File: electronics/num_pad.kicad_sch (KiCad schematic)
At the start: 37 parts, among them J10 Conn_01x05_Male, J9 Conn_01x05_Female, SW69 SW_SPST, SW70 SW_SPST, SW71 SW_SPST, SW72 SW_SPST, SW73 SW_SPST, SW74 SW_SPST, SW75 SW_SPST, SW76 SW_SPST, SW77 SW_SPST, SW78 SW_SPST, SW79 SW_SPST, SW80 SW_SPST, SW81 SW_SPST, SW82 SW_SPST, SW83 SW_SPST, SW84 SW_SPST, SW85 SW_SPST, U5 PCA9675PW

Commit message: finish matrix
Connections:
- net COL30: now also U5.16 (P13); no longer U5.13 (P10)
- net COL31: now also U5.15 (P12); no longer U5.14 (P11)
- net COL32: now also U5.14 (P11); no longer U5.15 (P12)
- net COL33: now also U5.13 (P10); no longer U5.16 (P13)
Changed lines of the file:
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@@
     (stroke (width 0) (type default) (color 0 0 0 0))
   )
+  (global_label "COL30" (shape input) (at 237.49 66.04 0) (fields_autoplaced)
+    (effects (font (size 1.27 1.27)) (justify left))
+    (property "Intersheet References" "${INTERSHEET_REFS}" (id 0) (at 245.9507 65.9606 0)
+      (effects (font (size 1.27 1.27)) (justify left) hide)
+    )
+  )
   (global_label "ROW30" (shape input) (at 55.88 101.6 180) (fields_autoplaced)
     (effects (font (size 1.27 1.27)) (justify right))
@@
     )
   )
-  (global_label "COL32" (shape input) (at 237.49 63.5 0) (fields_autoplaced)
-    (effects (font (size 1.27 1.27)) (justify left))
-    (property "Intersheet References" "${INTERSHEET_REFS}" (id 0) (at 245.9507 63.5794 0)
-      (effects (font (size 1.27 1.27)) (justify left) hide)
-    )
-  )
   (global_label "ROW34" (shape input) (at 96.52 165.1 180) (fields_autoplaced)
     (effects (font (size 1.27 1.27)) (justify right))
@@
     )
   )
+  (global_label "COL33" (shape input) (at 237.49 58.42 0) (fields_autoplaced)
+    (effects (font (size 1.27 1.27)) (justify left))
+    (property "Intersheet References" "${INTERSHEET_REFS}" (id 0) (at 245.9507 58.3406 0)
+      (effects (font (size 1.27 1.27)) (justify left) hide)
+    )
+  )
   (global_label "ROW30" (shape input) (at 96.52 101.6 180) (fields_autoplaced)
     (effects (font (size 1.27 1.27)) (justify right))
@@
     )
   )
-  (global_label "COL31" (shape input) (at 237.49 60.96 0) (fields_autoplaced)
-    (effects (font (size 1.27 1.27)) (justify left))
-    (property "Intersheet References" "${INTERSHEET_REFS}" (id 0) (at 245.9507 61.0394 0)
-      (effects (font (size 1.27 1.27)) (justify left) hide)
-    )
-  )
   (global_label "COL33" (shape input) (at 127 82.55 180) (fields_autoplaced)
     (effects (font (size 1.27 1.27)) (justify right))
@@
     )
   )
-  (global_label "COL30" (shape input) (at 237.49 58.42 0) (fields_autoplaced)
-    (effects (font (size 1.27 1.27)) (justify left))
-    (property "Intersheet References" "${INTERSHEET_REFS}" (id 0) (at 245.9507 58.4994 0)
-      (effects (font (size 1.27 1.27)) (justify left) hide)
-    )
-  )
   (global_label "~{INT}" (shape input) (at 237.49 45.72 0) (fields_autoplaced)
     (effects (font (size 1.27 1.27)) (justify left))
@@
     )
   )
-  (global_label "COL33" (shape input) (at 237.49 66.04 0) (fields_autoplaced)
-    (effects (font (size 1.27 1.27)) (justify left))
-    (property "Intersheet References" "${INTERSHEET_REFS}" (id 0) (at 245.9507 66.1194 0)
-      (effects (font (size 1.27 1.27)) (justify left) hide)
-    )
-  )
   (global_label "ROW33" (shape input) (at 76.2 149.86 180) (fields_autoplaced)
     (effects (font (size 1.27 1.27)) (justify right))
@@
     )
   )
+  (global_label "COL31" (shape input) (at 237.49 63.5 0) (fields_autoplaced)
+    (effects (font (size 1.27 1.27)) (justify left))
+    (property "Intersheet References" "${INTERSHEET_REFS}" (id 0) (at 245.9507 63.4206 0)
+      (effects (font (size 1.27 1.27)) (justify left) hide)
+    )
+  )
   (global_label "ROW33" (shape input) (at 201.93 66.04 180) (fields_autoplaced)
     (effects (font (size 1.27 1.27)) (justify right))
@@
       (effects (font (size 1.27 1.27)) (justify left) hide)
     )
+  )
+  (global_label "COL32" (shape input) (at 237.49 60.96 0) (fields_autoplaced)
+    (effects (font (size 1.27 1.27)) (justify left))
+    (property "Intersheet References" "${INTERSHEET_REFS}" (id 0) (at 245.9507 60.8806 0)
+      (effects (font (size 1.27 1.27)) (justify left) hide)
+    )

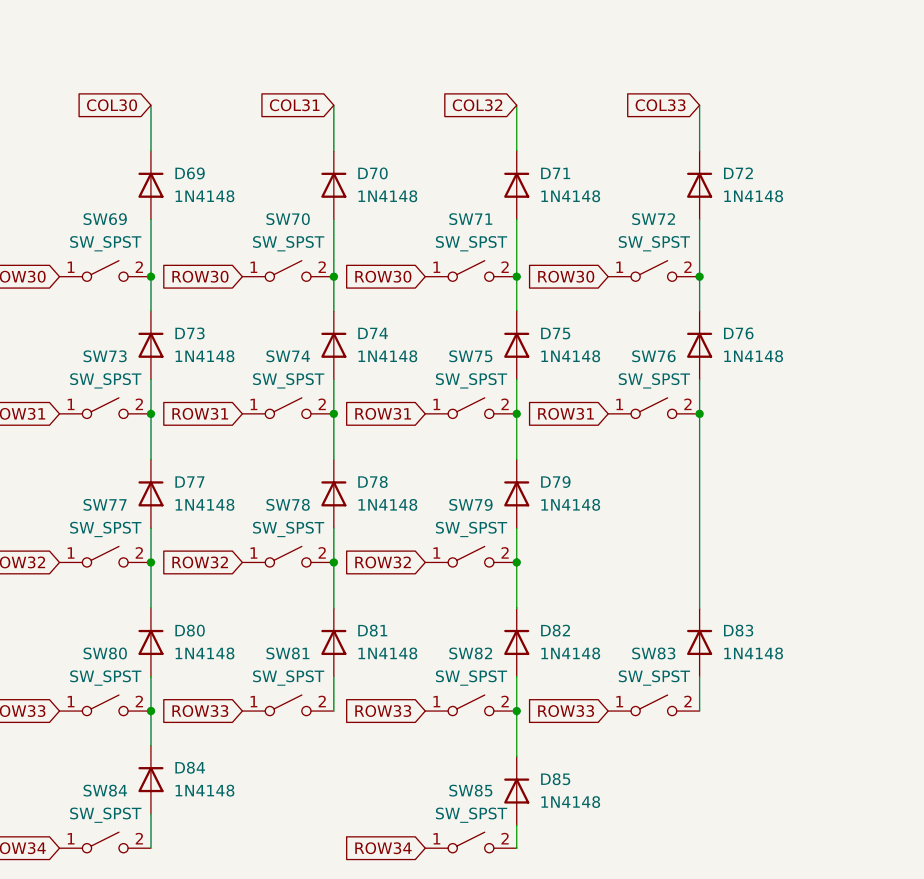
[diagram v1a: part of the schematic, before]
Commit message: update diode libraries
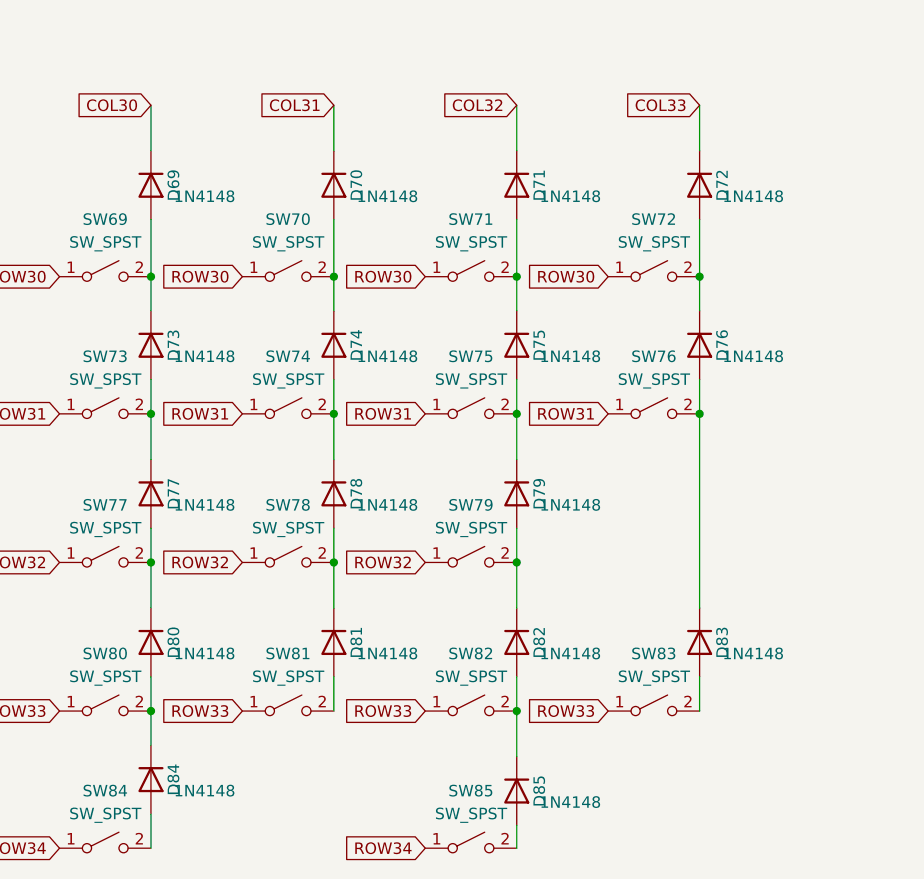
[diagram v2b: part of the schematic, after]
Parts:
- D69, D70, D71, D72, D73, D74, D75, D76, D77, D78, D79, D80, D81, D82, D83, D84, D85: symbol Diode:1N4148W -> 1N4148:1N4148

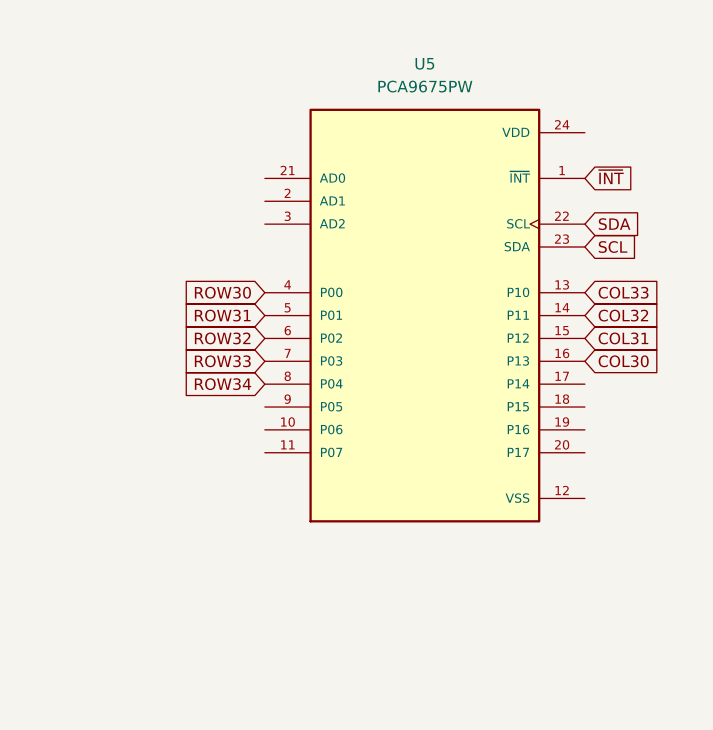
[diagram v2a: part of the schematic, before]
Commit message: add power and i2c addressing
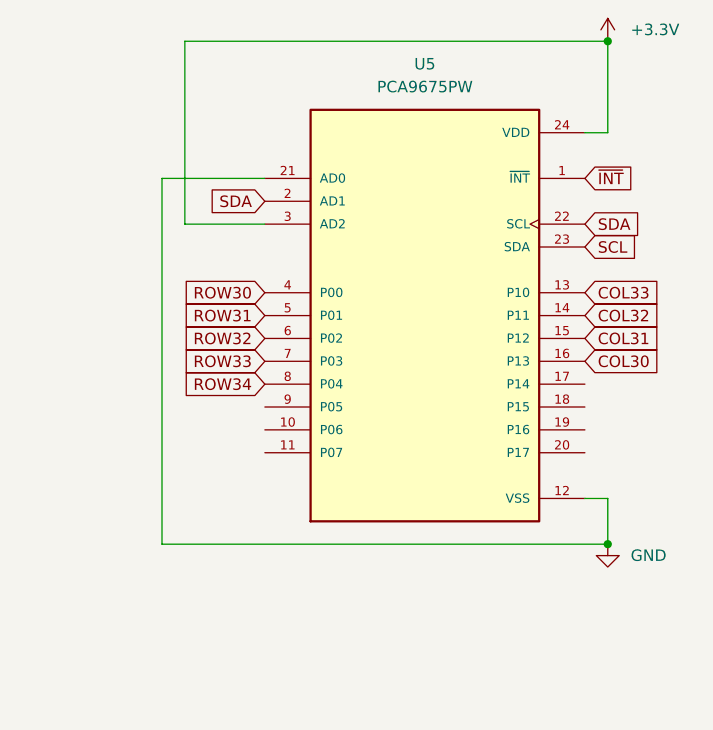
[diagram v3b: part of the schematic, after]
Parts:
- D69, D70, D71, D72, D73, D74, D75, D76, D77, D78, D79, D80, D81, D82, D83, D84, D85: footprint Diode_SMD:D_SOD-123 -> 1N4148:1N4148
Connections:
- net +3V3: now also U5.24 (VDD), U5.3 (AD2)
- net GND: now also U5.12 (VSS), U5.21 (AD0)
- net SDA: now also U5.2 (AD1)
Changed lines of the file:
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@@
   (junction (at 86.36 116.84) (diameter 0) (color 0 0 0 0)
   )
+  (junction (at 240.03 86.36) (diameter 0) (color 0 0 0 0)
+  )
   (junction (at 86.36 101.6) (diameter 0) (color 0 0 0 0)
   )
@@
   (junction (at 66.04 116.84) (diameter 0) (color 0 0 0 0)
   )
+  (junction (at 240.03 30.48) (diameter 0) (color 0 0 0 0)
+  )
   (wire (pts (xy 66.04 129.54) (xy 66.04 133.35))
     (stroke (width 0) (type default) (color 0 0 0 0))
   )
+  (wire (pts (xy 237.49 40.64) (xy 240.03 40.64))
+    (stroke (width 0) (type default) (color 0 0 0 0))
+  )
   (wire (pts (xy 106.68 129.54) (xy 106.68 133.35))
     (stroke (width 0) (type default) (color 0 0 0 0))
@@
     (stroke (width 0) (type default) (color 0 0 0 0))
   )
+  (wire (pts (xy 240.03 81.28) (xy 237.49 81.28))
+    (stroke (width 0) (type default) (color 0 0 0 0))
+  )
   (wire (pts (xy 106.68 82.55) (xy 106.68 87.63))
     (stroke (width 0) (type default) (color 0 0 0 0))
@@
     (stroke (width 0) (type default) (color 0 0 0 0))
   )
+  (wire (pts (xy 201.93 45.72) (xy 190.5 45.72))
+    (stroke (width 0) (type default) (color 0 0 0 0))
+  )
   (wire (pts (xy 106.68 101.6) (xy 106.68 105.41))
     (stroke (width 0) (type default) (color 0 0 0 0))
@@
     (stroke (width 0) (type default) (color 0 0 0 0))
   )
+  (wire (pts (xy 190.5 86.36) (xy 240.03 86.36))
+    (stroke (width 0) (type default) (color 0 0 0 0))
+  )
   (wire (pts (xy 127 82.55) (xy 127 87.63))
     (stroke (width 0) (type default) (color 0 0 0 0))
@@
     (stroke (width 0) (type default) (color 0 0 0 0))
   )
+  (wire (pts (xy 193.04 30.48) (xy 193.04 50.8))
+    (stroke (width 0) (type default) (color 0 0 0 0))
+  )
+  (wire (pts (xy 240.03 30.48) (xy 193.04 30.48))
+    (stroke (width 0) (type default) (color 0 0 0 0))
+  )
   (wire (pts (xy 66.04 146.05) (xy 66.04 149.86))
     (stroke (width 0) (type default) (color 0 0 0 0))
@@
   )
   (wire (pts (xy 86.36 95.25) (xy 86.36 101.6))
+    (stroke (width 0) (type default) (color 0 0 0 0))
+  )
+  (wire (pts (xy 240.03 86.36) (xy 240.03 81.28))
+    (stroke (width 0) (type default) (color 0 0 0 0))
+  )
+  (wire (pts (xy 190.5 45.72) (xy 190.5 86.36))
+    (stroke (width 0) (type default) (color 0 0 0 0))
+  )
+  (wire (pts (xy 193.04 50.8) (xy 201.93 50.8))
+    (stroke (width 0) (type default) (color 0 0 0 0))
+  )
+  (wire (pts (xy 240.03 40.64) (xy 240.03 30.48))
     (stroke (width 0) (type default) (color 0 0 0 0))
   )
@@
     )
   )
+  (global_label "SDA" (shape input) (at 201.93 48.26 180) (fields_autoplaced)
+    (effects (font (size 1.27 1.27)) (justify right))
+    (property "Intersheet References" "${INTERSHEET_REFS}" (id 0) (at 195.9488 48.1806 0)
+      (effects (font (size 1.27 1.27)) (justify right) hide)
+    )
+  )
   (global_label "~{INT}" (shape input) (at 237.49 45.72 0) (fields_autoplaced)
     (effects (font (size 1.27 1.27)) (justify left))
@@
       (effects (font (size 1.27 1.27)) (justify left))
     )
-    (property "Footprint" "Diode_SMD:D_SOD-123" (id 2) (at 81.915 91.44 0)
+    (property "Footprint" "1N4148:1N4148" (id 2) (at 81.915 91.44 0)
       (effects (font (size 1.27 1.27)) hide)
     )
@@
       (effects (font (size 1.27 1.27)) (justify left))
     )
-    (property "Footprint" "Diode_SMD:D_SOD-123" (id 2) (at 61.595 142.24 0)
+    (property "Footprint" "1N4148:1N4148" (id 2) (at 61.595 142.24 0)
       (effects (font (size 1.27 1.27)) hide)
     )
@@
       (effects (font (size 1.27 1.27)) (justify left))
     )
-    (property "Footprint" "Diode_SMD:D_SOD-123" (id 2) (at 81.915 125.73 0)
+    (property "Footprint" "1N4148:1N4148" (id 2) (at 81.915 125.73 0)
       (effects (font (size 1.27 1.27)) hide)
     )
@@
     (pin "2")
   )
+  (symbol (lib_id "power:GND") (at 240.03 86.36 0) (unit 1)
+    (in_bom yes) (on_board yes) (fields_autoplaced)
+    (property "Reference" "#PWR?" (id 0) (at 240.03 92.71 0)
+      (effects (font (size 1.27 1.27)) hide)
+    )
+    (property "Value" "GND" (id 1) (at 242.57 87.6299 0)
+      (effects (font (size 1.27 1.27)) (justify left))
+    )
+    (property "Footprint" "" (id 2) (at 240.03 86.36 0)
+      (effects (font (size 1.27 1.27)) hide)
+    )
+    (property "Datasheet" "" (id 3) (at 240.03 86.36 0)
+      (effects (font (size 1.27 1.27)) hide)
+    )
+    (pin "1")
+  )
   (symbol (lib_name "1N4148_11") (lib_id "1N4148:1N4148") (at 127 91.44 270) (unit 1)
     (in_bom yes) (on_board yes) (fields_autoplaced)
@@
       (effects (font (size 1.27 1.27)) (justify left))
     )
-    (property "Footprint" "Diode_SMD:D_SOD-123" (id 2) (at 122.555 91.44 0)
+    (property "Footprint" "1N4148:1N4148" (id 2) (at 122.555 91.44 0)
       (effects (font (size 1.27 1.27)) hide)
     )
@@
       (effects (font (size 1.27 1.27)) (justify left))
     )
-    (property "Footprint" "Diode_SMD:D_SOD-123" (id 2) (at 102.235 158.75 0)
+    (property "Footprint" "1N4148:1N4148" (id 2) (at 102.235 158.75 0)
       (effects (font (size 1.27 1.27)) hide)
     )
@@
       (effects (font (size 1.27 1.27)) (justify left))
     )
-    (property "Footprint" "Diode_SMD:D_SOD-123" (id 2) (at 61.595 157.48 0)
+    (property "Footprint" "1N4148:1N4148" (id 2) (at 61.595 157.48 0)
       (effects (font (size 1.27 1.27)) hide)
     )
@@
       (effects (font (size 1.27 1.27)) (justify left))
     )
-    (property "Footprint" "Diode_SMD:D_SOD-123" (id 2) (at 81.915 142.24 0)
+    (property "Footprint" "1N4148:1N4148" (id 2) (at 81.915 142.24 0)
       (effects (font (size 1.27 1.27)) hide)
     )
@@
       (effects (font (size 1.27 1.27)) (justify left))
     )
-    (property "Footprint" "Diode_SMD:D_SOD-123" (id 2) (at 102.235 91.44 0)
+    (property "Footprint" "1N4148:1N4148" (id 2) (at 102.235 91.44 0)
       (effects (font (size 1.27 1.27)) hide)
     )
@@
       (effects (font (size 1.27 1.27)) (justify left))
     )
-    (property "Footprint" "Diode_SMD:D_SOD-123" (id 2) (at 102.235 142.24 0)
+    (property "Footprint" "1N4148:1N4148" (id 2) (at 102.235 142.24 0)
       (effects (font (size 1.27 1.27)) hide)
     )
@@
       (effects (font (size 1.27 1.27)) (justify left))
     )
-    (property "Footprint" "Diode_SMD:D_SOD-123" (id 2) (at 81.915 109.22 0)
+    (property "Footprint" "1N4148:1N4148" (id 2) (at 81.915 109.22 0)
       (effects (font (size 1.27 1.27)) hide)
     )
@@
       (effects (font (size 1.27 1.27)) (justify left))
     )
-    (property "Footprint" "Diode_SMD:D_SOD-123" (id 2) (at 61.595 109.22 0)
+    (property "Footprint" "1N4148:1N4148" (id 2) (at 61.595 109.22 0)
       (effects (font (size 1.27 1.27)) hide)
     )
@@
       (effects (font (size 1.27 1.27)) (justify left))
     )
-    (property "Footprint" "Diode_SMD:D_SOD-123" (id 2) (at 61.595 125.73 0)
+    (property "Footprint" "1N4148:1N4148" (id 2) (at 61.595 125.73 0)
       (effects (font (size 1.27 1.27)) hide)
     )
@@
       (effects (font (size 1.27 1.27)) (justify left))
     )
-    (property "Footprint" "Diode_SMD:D_SOD-123" (id 2) (at 122.555 109.22 0)
+    (property "Footprint" "1N4148:1N4148" (id 2) (at 122.555 109.22 0)
       (effects (font (size 1.27 1.27)) hide)
     )
@@
     (pin "1")
     (pin "2")
+  )
+  (symbol (lib_id "power:+3.3V") (at 240.03 30.48 0) (unit 1)
+    (in_bom yes) (on_board yes) (fields_autoplaced)
+    (property "Reference" "#PWR?" (id 0) (at 240.03 34.29 0)
+      (effects (font (size 1.27 1.27)) hide)
+    )
+    (property "Value" "+3.3V" (id 1) (at 242.57 29.2099 0)
+      (effects (font (size 1.27 1.27)) (justify left))
+    )
+    (property "Footprint" "" (id 2) (at 240.03 30.48 0)
+      (effects (font (size 1.27 1.27)) hide)
+    )
+    (property "Datasheet" "" (id 3) (at 240.03 30.48 0)
+      (effects (font (size 1.27 1.27)) hide)
+    )
+    (pin "1")
   )
   (symbol (lib_name "SW_SPST_24") (lib_id "Kailh:SW_SPST") (at 60.96 165.1 0) (unit 1)
@@
       (effects (font (size 1.27 1.27)) (justify left))
     )
-    (property "Footprint" "Diode_SMD:D_SOD-123" (id 2) (at 102.235 125.73 0)
+    (property "Footprint" "1N4148:1N4148" (id 2) (at 102.235 125.73 0)
       (effects (font (size 1.27 1.27)) hide)
     )
@@
       (effects (font (size 1.27 1.27)) (justify left))
     )
-    (property "Footprint" "Diode_SMD:D_SOD-123" (id 2) (at 61.595 91.44 0)
+    (property "Footprint" "1N4148:1N4148" (id 2) (at 61.595 91.44 0)
       (effects (font (size 1.27 1.27)) hide)
     )
@@
       (effects (font (size 1.27 1.27)) (justify left))
     )
-    (property "Footprint" "Diode_SMD:D_SOD-123" (id 2) (at 102.235 109.22 0)
+    (property "Footprint" "1N4148:1N4148" (id 2) (at 102.235 109.22 0)
       (effects (font (size 1.27 1.27)) hide)
     )
@@
       (effects (font (size 1.27 1.27)) (justify left))
     )
-    (property "Footprint" "Diode_SMD:D_SOD-123" (id 2) (at 122.555 142.24 0)
-      (effects (font (size 1.27 1.27)) hide)
-    )
+    (property "Footprint" "1N4148:1N4148" (id 2) (at 122.555 142.24 0)
+      (effects (font (size 1.27 1.27)) hide)
+    )
